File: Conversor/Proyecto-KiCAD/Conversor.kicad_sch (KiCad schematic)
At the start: 21 parts, among them J1 ConnPila, J2 ConnTrafoP, J3 ConnTrafoS, J4 ConnLf, J5 ConnCarga, Q1 IRFP150, Q2 IRFP150, Q3 IRFP150, Q4 IRFP150

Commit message: Comenzar a asignar footprints a todos los componentes
- Agregado un header para conectar el módulo de tarjeta SD de Arduino
por SPI
- Los GNDs conectados por resistencias nulas son para conectar los GNDs
en caso de que fuera necesario
- Agregar una nota de aplicaión de aislación para I2C (creo que como
estan conectados SDAO y SDAI está bien)
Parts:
- C1, C17, C2, C3, C4: footprint (none) -> Capacitor_SMD:C_1206_3216Metric_Pad1.33x1.80mm_HandSolder
- R7: footprint (none) -> Resistor_SMD:R_2512_6332Metric_Pad1.40x3.35mm_HandSolder
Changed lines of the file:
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@@
       (effects (font (size 1.27 1.27)) (justify left))
     )
-    (property "Footprint" "" (id 2) (at 105.41 113.03 0)
+    (property "Footprint" "Capacitor_SMD:C_1206_3216Metric_Pad1.33x1.80mm_HandSolder" (id 2) (at 105.41 113.03 0)
       (effects (font (size 1.27 1.27)) hide)
     )
@@
       (effects (font (size 1.27 1.27)) (justify left))
     )
-    (property "Footprint" "" (id 2) (at 154.94 113.03 0)
+    (property "Footprint" "Capacitor_SMD:C_1206_3216Metric_Pad1.33x1.80mm_HandSolder" (id 2) (at 154.94 113.03 0)
       (effects (font (size 1.27 1.27)) hide)
     )
@@
       (effects (font (size 1.27 1.27)) (justify left))
     )
-    (property "Footprint" "" (id 2) (at 154.94 87.63 0)
+    (property "Footprint" "Capacitor_SMD:C_1206_3216Metric_Pad1.33x1.80mm_HandSolder" (id 2) (at 154.94 87.63 0)
       (effects (font (size 1.27 1.27)) hide)
     )
@@
     (property "Reference" "C17" (id 0) (at 50.8063 76.2 90))
     (property "Value" "CS" (id 1) (at 50.8063 78.74 90))
-    (property "Footprint" "" (id 2) (at 50.8 82.55 0)
+    (property "Footprint" "Capacitor_SMD:C_1206_3216Metric_Pad1.33x1.80mm_HandSolder" (id 2) (at 50.8 82.55 0)
       (effects (font (size 1.27 1.27)) hide)
     )
@@
     (property "Reference" "R7" (id 0) (at 46.99 91.44 90))
     (property "Value" "RS" (id 1) (at 50.8 92.71 90))
-    (property "Footprint" "" (id 2) (at 50.8 91.948 90)
+    (property "Footprint" "Resistor_SMD:R_2512_6332Metric_Pad1.40x3.35mm_HandSolder" (id 2) (at 50.8 91.948 90)
       (effects (font (size 1.27 1.27)) hide)
     )
@@
       (effects (font (size 1.27 1.27)) (justify left))
     )
-    (property "Footprint" "" (id 2) (at 105.41 87.63 0)
-      (effects (font (size 1.27 1.27)) hide)
-    )
+    (property "Footprint" "Capacitor_SMD:C_1206_3216Metric_Pad1.33x1.80mm_HandSolder" (id 2) (at 105.41 87.63 0)
+      (effects (font (size 1.27 1.27)) hide)
+    )

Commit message: Comenzar el layout de componentes de la PCB
- Todos los componentes con footprints asignados (preliminar)
- Organizados los componentes de la placa adaptadora en el esquema del
PCB (usando como guia aproximada la placa adaptadora)
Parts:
- C5: footprint (none) -> Capacitor_THT:CP_Radial_D6.3mm_P2.50mm
- C6: footprint (none) -> Capacitor_THT:CP_Radial_D18.0mm_P7.50mm
- J1, J2, J3, J4, J5: footprint (none) -> TerminalBlock:TerminalBlock_bornier-2_P5.08mm
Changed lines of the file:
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@@
       (effects (font (size 1.27 1.27)) (justify right))
     )
-    (property "Footprint" "" (id 2) (at 67.31 99.06 0)
+    (property "Footprint" "Capacitor_THT:CP_Radial_D6.3mm_P2.50mm" (id 2) (at 67.31 99.06 0)
       (effects (font (size 1.27 1.27)) hide)
     )
@@
       (effects (font (size 1.27 1.27)) (justify left))
     )
-    (property "Footprint" "" (id 2) (at 29.21 97.79 0)
+    (property "Footprint" "TerminalBlock:TerminalBlock_bornier-2_P5.08mm" (id 2) (at 29.21 97.79 0)
       (effects (font (size 1.27 1.27)) hide)
     )
@@
       (effects (font (size 1.27 1.27)) (justify right))
     )
-    (property "Footprint" "" (id 2) (at 229.87 78.74 0)
+    (property "Footprint" "TerminalBlock:TerminalBlock_bornier-2_P5.08mm" (id 2) (at 229.87 78.74 0)
       (effects (font (size 1.27 1.27)) hide)
     )
@@
     (property "Reference" "J3" (id 0) (at 186.69 95.25 0))
     (property "Value" "ConnTrafoS" (id 1) (at 186.69 102.87 0))
-    (property "Footprint" "" (id 2) (at 186.69 97.79 0)
+    (property "Footprint" "TerminalBlock:TerminalBlock_bornier-2_P5.08mm" (id 2) (at 186.69 97.79 0)
       (effects (font (size 1.27 1.27)) hide)
     )
@@
       (effects (font (size 1.27 1.27)) (justify left))
     )
-    (property "Footprint" "" (id 2) (at 163.83 97.79 0)
+    (property "Footprint" "TerminalBlock:TerminalBlock_bornier-2_P5.08mm" (id 2) (at 163.83 97.79 0)
       (effects (font (size 1.27 1.27)) hide)
     )
@@
       (effects (font (size 1.27 1.27)) (justify left))
     )
-    (property "Footprint" "" (id 2) (at 270.51 99.06 0)
+    (property "Footprint" "TerminalBlock:TerminalBlock_bornier-2_P5.08mm" (id 2) (at 270.51 99.06 0)
       (effects (font (size 1.27 1.27)) hide)
     )
@@
       (effects (font (size 1.27 1.27)) (justify left))
     )
-    (property "Footprint" "" (id 2) (at 253.6952 104.14 0)
-      (effects (font (size 1.27 1.27)) hide)
-    )
+    (property "Footprint" "Capacitor_THT:CP_Radial_D18.0mm_P7.50mm" (id 2) (at 253.6952 104.14 0)
+      (effects (font (size 1.27 1.27)) hide)
+    )

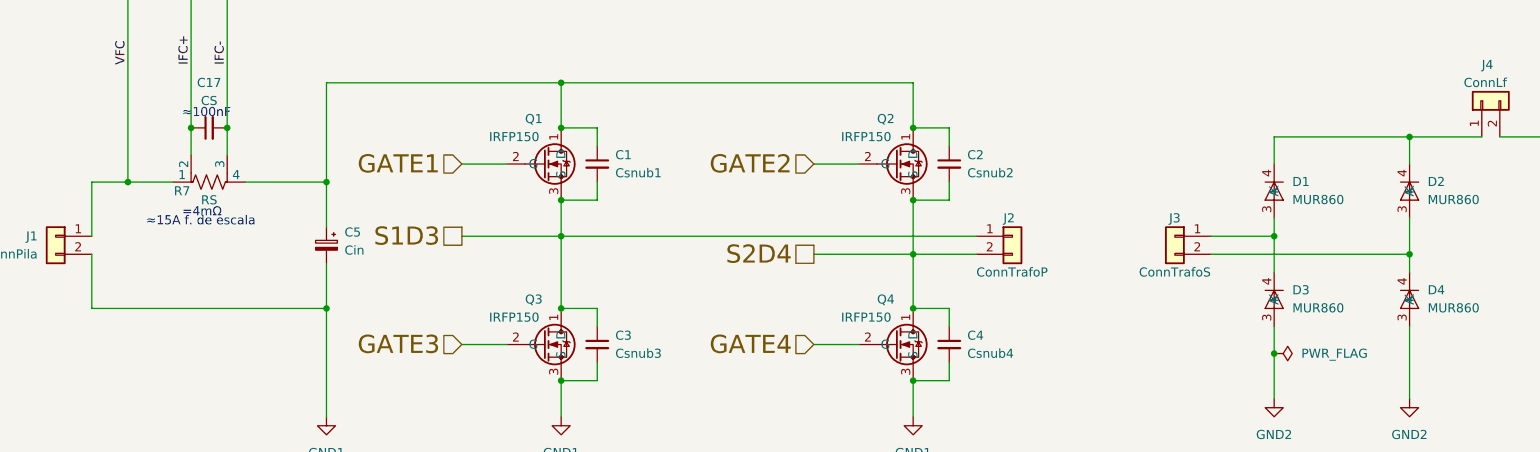
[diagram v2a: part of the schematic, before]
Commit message: Reempezar el ordenado de componentes del PCB
- Intentar copiar mas a la placa adaptadora en la parte del DSP (digital)
  - Algunas cosas (como los headers y la parte de USB) se movieron para hacer entrar mejor las cosas
- Layout bastante completo
- Agregados algunos modelos 3D faltantes
Por hacer:
  - Mover y reorganizar la parte del LM5056, porque tiene una pata que va al secundario, y ahora esta muy lejos del area de GND2
  - Ver como reorganizar un poco para que no queden esquinas vacias
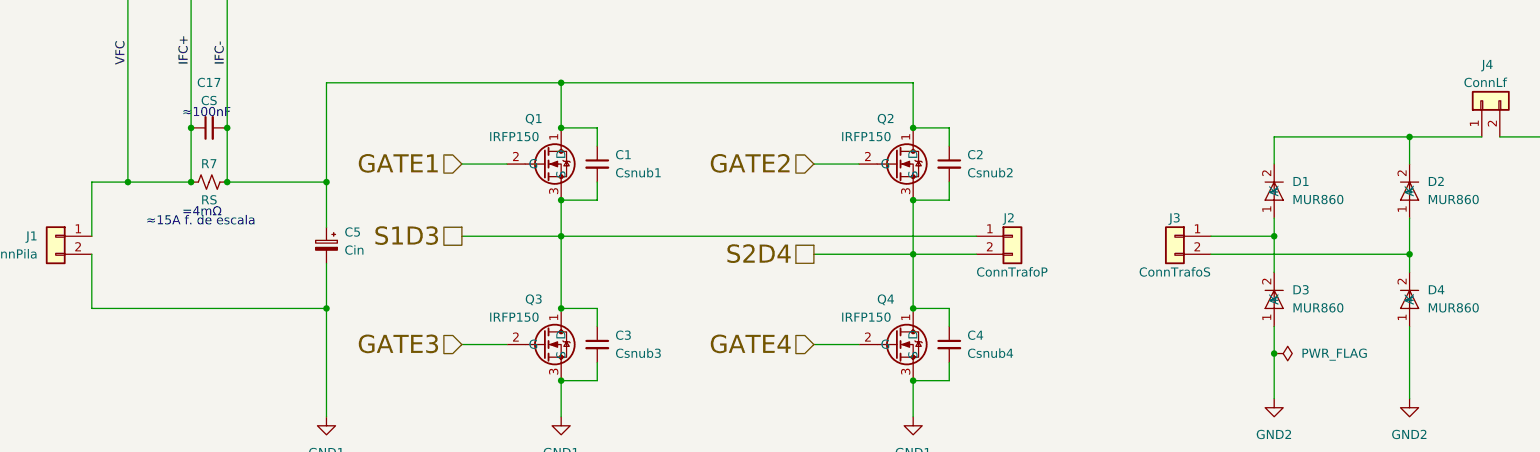
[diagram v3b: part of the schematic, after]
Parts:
- removed R7: RS, Resistor_SMD:R_2512_6332Metric_Pad1.40x3.35mm_HandSolder, symbol Device:R_Shunt_US
- added R7: RS, Resistor_SMD:R_2512_6332Metric_Pad1.40x3.35mm_HandSolder, symbol Device:R_Small_US
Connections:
- net VFC is gone; now on net IFC+: J1.1 (Pin_1)
- net GND2: now also D3.1 (A), D4.1 (A); no longer D3.3 (A), D4.3 (A)
- net IFC+: now also R7.1
- net IFC-: now also C1.1, C2.1, C5.1, Q1.1 (D), Q2.1 (D), R7.2
- new net: D1.1 (A), D3.2 (K), J3.1 (Pin_1)
- new net: D1.2 (K), D2.2 (K), J4.1 (Pin_1)
- new net: D2.1 (A), D4.2 (K), J3.2 (Pin_2)
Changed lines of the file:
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@@
 (kicad_sch (version 20211123) (generator eeschema)
   (paper "A4")
+  (junction (at 53.34 90.17) (diameter 0) (color 0 0 0 0)
+  )
+  (junction (at 48.26 90.17) (diameter 0) (color 0 0 0 0)
+  )
   (junction (at 67.31 90.17) (diameter 0) (color 0 0 0 0)
   )
@@
     (stroke (width 0) (type default) (color 0 0 0 0))
   )
-  (wire (pts (xy 39.37 90.17) (xy 45.72 90.17))
+  (wire (pts (xy 39.37 90.17) (xy 48.26 90.17))
     (stroke (width 0) (type default) (color 0 0 0 0))
   )
@@
     (stroke (width 0) (type default) (color 0 0 0 0))
   )
-  (wire (pts (xy 55.88 90.17) (xy 67.31 90.17))
+  (wire (pts (xy 53.34 90.17) (xy 67.31 90.17))
     (stroke (width 0) (type default) (color 0 0 0 0))
   )
@@
     (stroke (width 0) (type default) (color 0 0 0 0))
   )
-  (wire (pts (xy 48.26 82.55) (xy 48.26 86.36))
+  (wire (pts (xy 48.26 82.55) (xy 48.26 90.17))
     (stroke (width 0) (type default) (color 0 0 0 0))
   )
@@
     (stroke (width 0) (type default) (color 0 0 0 0))
   )
-  (wire (pts (xy 53.34 82.55) (xy 53.34 86.36))
+  (wire (pts (xy 53.34 82.55) (xy 53.34 90.17))
     (stroke (width 0) (type default) (color 0 0 0 0))
   )
@@
     (pin "2")
   )
+  (symbol (lib_id "Device:R_Small_US") (at 50.8 90.17 90) (unit 1)
+    (in_bom yes) (on_board yes)
+    (property "Reference" "R7" (id 0) (at 50.8 87.63 90))
+    (property "Value" "RS" (id 1) (at 50.8 92.71 90))
+    (property "Footprint" "Resistor_SMD:R_2512_6332Metric_Pad1.40x3.35mm_HandSolder" (id 2) (at 50.8 90.17 0)
+      (effects (font (size 1.27 1.27)) hide)
+    )
+    (property "Datasheet" "~" (id 3) (at 50.8 90.17 0)
+      (effects (font (size 1.27 1.27)) hide)
+    )
+    (pin "1")
+    (pin "2")
+  )
   (symbol (lib_id "power:GND2") (at 252.73 120.65 0) (unit 1)
     (in_bom yes) (on_board yes) (fields_autoplaced)
@@
       (effects (font (size 1.27 1.27)) hide)
     )
-    (pin "3")
-    (pin "4")
-  )
-  (symbol (lib_id "Componentes proyecto:MUR860") (at 200.66 91.44 0) (unit 1)
+    (pin "1")
+    (pin "2")
+  )
+  (symbol (lib_name "MUR860_1") (lib_id "Componentes proyecto:MUR860") (at 200.66 91.44 0) (unit 1)
     (in_bom yes) (on_board yes) (fields_autoplaced)
     (property "Reference" "D1" (id 0) (at 203.2 90.1318 0)
@@
       (effects (font (size 1.27 1.27)) hide)
     )
-    (pin "3")
-    (pin "4")
+    (pin "1")
+    (pin "2")
   )
   (symbol (lib_id "power:GND2") (at 265.43 120.65 0) (unit 1)
@@
     (pin "2")
   )
-  (symbol (lib_id "Componentes proyecto:MUR860") (at 219.71 91.44 0) (unit 1)
+  (symbol (lib_name "MUR860_2") (lib_id "Componentes proyecto:MUR860") (at 219.71 91.44 0) (unit 1)
     (in_bom yes) (on_board yes) (fields_autoplaced)
     (property "Reference" "D2" (id 0) (at 222.25 90.1318 0)
@@
       (effects (font (size 1.27 1.27)) hide)
     )
-    (pin "3")
-    (pin "4")
-  )
-  (symbol (lib_id "Device:R_Shunt_US") (at 50.8 90.17 90) (unit 1)
-    (in_bom yes) (on_board yes)
-    (property "Reference" "R7" (id 0) (at 46.99 91.44 90))
-    (property "Value" "RS" (id 1) (at 50.8 92.71 90))
-    (property "Footprint" "Resistor_SMD:R_2512_6332Metric_Pad1.40x3.35mm_HandSolder" (id 2) (at 50.8 91.948 90)
-      (effects (font (size 1.27 1.27)) hide)
-    )
-    (property "Datasheet" "~" (id 3) (at 50.8 90.17 0)
-      (effects (font (size 1.27 1.27)) hide)
-    )
-    (pin "1")
-    (pin "2")
-    (pin "3")
-    (pin "4")
+    (pin "1")
+    (pin "2")
   )
   (symbol (lib_id "power:GND1") (at 149.86 123.19 0) (unit 1)
@@
     (pin "2")
   )
-  (symbol (lib_id "Componentes proyecto:MUR860") (at 219.71 106.68 0) (unit 1)
+  (symbol (lib_name "MUR860_3") (lib_id "Componentes proyecto:MUR860") (at 219.71 106.68 0) (unit 1)
     (in_bom yes) (on_board yes) (fields_autoplaced)
     (property "Reference" "D4" (id 0) (at 222.25 105.3718 0)
@@
       (effects (font (size 1.27 1.27)) hide)
     )
-    (pin "3")
-    (pin "4")
+    (pin "1")
+    (pin "2")
   )
   (symbol (lib_id "Device:C_Small") (at 105.41 87.63 0) (unit 1)

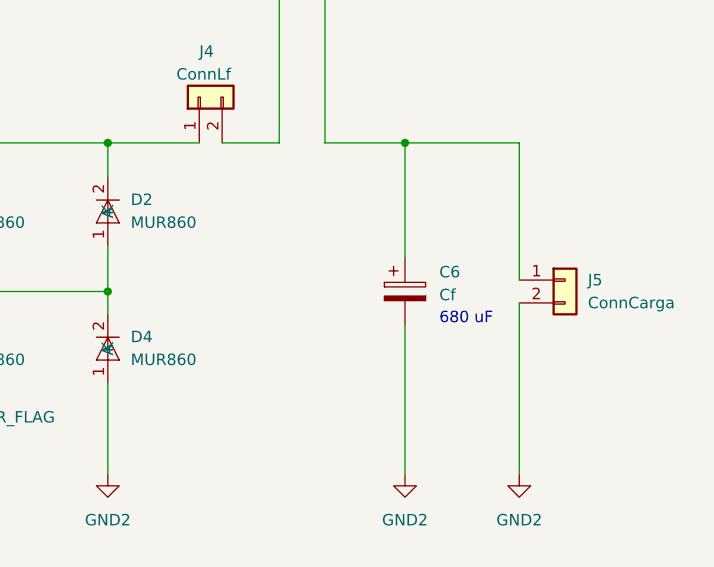
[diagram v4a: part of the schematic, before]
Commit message: Continuar con el diseño de la PCB
- Agregar los agujeros de tornillos
- Terminar la parte del secundario
- Agregar el borde en Egde.cuts que causaba problema
- Corregir las pista que no entran derechas a los pads
- Cambiar las footprints de los conectores
Por hacer:
  - Consultar de componentes como headers a Claus
  - Una vez terminada pedir cotización en las paginas que me pasó Jorge (Bookmarks de Firefox)
  - Ver de agrear un selector para la alimentación externa por header en la entrada de 12-18V (preguntar a Claus)
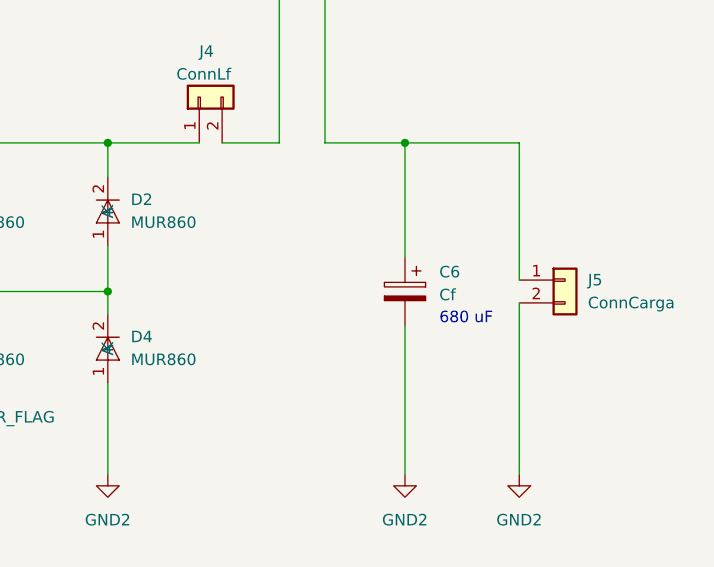
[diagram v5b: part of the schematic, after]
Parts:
- C5: footprint Capacitor_THT:CP_Radial_D6.3mm_P2.50mm -> Capacitor_THT:CP_Radial_D12.5mm_P5.00mm
- J1, J2, J3, J4, J5: footprint TerminalBlock:TerminalBlock_bornier-2_P5.08mm -> TerminalBlock:TerminalBlock_Wuerth_691311400102_P7.62mm
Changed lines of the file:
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@@
       (effects (font (size 1.27 1.27)) (justify right))
     )
-    (property "Footprint" "Capacitor_THT:CP_Radial_D6.3mm_P2.50mm" (id 2) (at 67.31 99.06 0)
+    (property "Footprint" "Capacitor_THT:CP_Radial_D12.5mm_P5.00mm" (id 2) (at 67.31 99.06 0)
       (effects (font (size 1.27 1.27)) hide)
     )
@@
       (effects (font (size 1.27 1.27)) (justify left))
     )
-    (property "Footprint" "TerminalBlock:TerminalBlock_bornier-2_P5.08mm" (id 2) (at 29.21 97.79 0)
+    (property "Footprint" "TerminalBlock:TerminalBlock_Wuerth_691311400102_P7.62mm" (id 2) (at 29.21 97.79 0)
       (effects (font (size 1.27 1.27)) hide)
     )
@@
       (effects (font (size 1.27 1.27)) (justify right))
     )
-    (property "Footprint" "TerminalBlock:TerminalBlock_bornier-2_P5.08mm" (id 2) (at 229.87 78.74 0)
+    (property "Footprint" "TerminalBlock:TerminalBlock_Wuerth_691311400102_P7.62mm" (id 2) (at 229.87 78.74 0)
       (effects (font (size 1.27 1.27)) hide)
     )
@@
     (property "Reference" "J3" (id 0) (at 186.69 95.25 0))
     (property "Value" "ConnTrafoS" (id 1) (at 186.69 102.87 0))
-    (property "Footprint" "TerminalBlock:TerminalBlock_bornier-2_P5.08mm" (id 2) (at 186.69 97.79 0)
+    (property "Footprint" "TerminalBlock:TerminalBlock_Wuerth_691311400102_P7.62mm" (id 2) (at 186.69 97.79 0)
       (effects (font (size 1.27 1.27)) hide)
     )
@@
       (effects (font (size 1.27 1.27)) (justify left))
     )
-    (property "Footprint" "TerminalBlock:TerminalBlock_bornier-2_P5.08mm" (id 2) (at 163.83 97.79 0)
+    (property "Footprint" "TerminalBlock:TerminalBlock_Wuerth_691311400102_P7.62mm" (id 2) (at 163.83 97.79 0)
       (effects (font (size 1.27 1.27)) hide)
     )
@@
       (effects (font (size 1.27 1.27)) (justify left))
     )
-    (property "Footprint" "TerminalBlock:TerminalBlock_bornier-2_P5.08mm" (id 2) (at 270.51 99.06 0)
+    (property "Footprint" "TerminalBlock:TerminalBlock_Wuerth_691311400102_P7.62mm" (id 2) (at 270.51 99.06 0)
       (effects (font (size 1.27 1.27)) hide)
     )
@@
     (pin "3")
   )
-  (symbol (lib_id "Device:C_Polarized") (at 252.73 100.33 0) (unit 1)
+  (symbol (lib_id "Device:C_Polarized") (at 252.73 100.33 0) (mirror y) (unit 1)
     (in_bom yes) (on_board yes) (fields_autoplaced)
     (property "Reference" "C6" (id 0) (at 256.54 98.1709 0)
-      (effects (font (size 1.27 1.27)) (justify left))
+      (effects (font (size 1.27 1.27)) (justify right))
     )
     (property "Value" "Cf" (id 1) (at 256.54 100.7109 0)
-      (effects (font (size 1.27 1.27)) (justify left))
-    )
-    (property "Footprint" "Capacitor_THT:CP_Radial_D18.0mm_P7.50mm" (id 2) (at 253.6952 104.14 0)
-      (effects (font (size 1.27 1.27)) hide)
-    )
+      (effects (font (size 1.27 1.27)) (justify right))
+    )
+    (property "Footprint" "Capacitor_THT:CP_Radial_D18.0mm_P7.50mm" (id 2) (at 251.7648 104.14 0)
+      (effects (font (size 1.27 1.27)) hide)
+    )

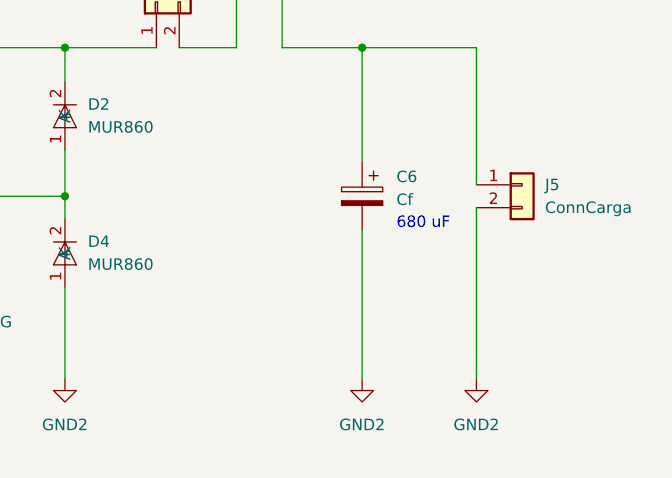
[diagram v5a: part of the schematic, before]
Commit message: Terminar de rutear todas las pistas de cobre de la placa
- Pistas de 4.5mm para las partes de 9A (primario) y 2mm para las de 4A (secundario)
- Agregar doble capacitor en serie a la salida, para disminuir los requerimientos de tensión de cada capacitor
  - Falta ver si es necesario a la entrada
- Agregar el circuito de medición de corriente a la entrada como recomienda la hoja de datos del LM5056
- Agregar modelos 3D de los conectores (sacados de Irusta-Caravelli)
Por hacer:
  - Preguntar por los componentes disponibles a Claus
  - Ver como entran los disipadores para MOSFETs y diodos
  - Asegurarse de la conexión de las dos líneas de datos de I2C despues del aislador
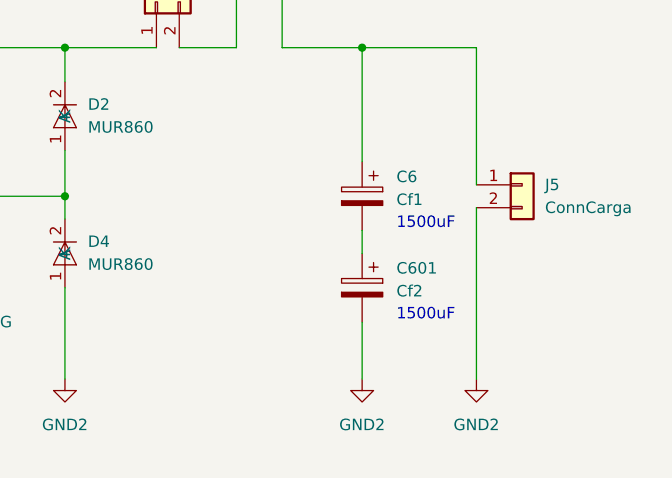
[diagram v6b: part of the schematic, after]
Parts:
- added C601: Cf2, Capacitor_THT:CP_Radial_D18.0mm_P7.50mm, symbol Device:C_Polarized
- C6: value Cf -> Cf1
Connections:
- net GND2: now also C601.2; no longer C6.2
- new net: C6.2, C601.1
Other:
- note added: "1500uF"
- note removed: "680 uF"
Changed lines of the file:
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@@
+    (stroke (width 0) (type default) (color 0 0 0 0))
+  )
+  (wire (pts (xy 252.73 114.3) (xy 252.73 120.65))
     (stroke (width 0) (type default) (color 0 0 0 0))
   )
@@
     (stroke (width 0) (type default) (color 0 0 0 0))
   )
-  (wire (pts (xy 252.73 104.14) (xy 252.73 120.65))
+  (wire (pts (xy 252.73 104.14) (xy 252.73 106.68))
     (stroke (width 0) (type default) (color 0 0 0 0))
   )
@@
     (effects (font (size 1.27 1.27)) (justify left bottom))
   )
-  (text "680 uF" (at 256.54 104.14 0)
+  (text "1500uF" (at 256.54 104.14 0)
     (effects (font (size 1.27 1.27)) (justify left bottom))
   )
   (text "≈15A f. de escala" (at 41.91 96.52 0)
+    (effects (font (size 1.27 1.27)) (justify left bottom))
+  )
+  (text "1500uF" (at 256.54 114.3 0)
     (effects (font (size 1.27 1.27)) (justify left bottom))
   )
@@
     (pin "3")
   )
+  (symbol (lib_id "Device:C_Polarized") (at 252.73 110.49 0) (mirror y) (unit 1)
+    (in_bom yes) (on_board yes) (fields_autoplaced)
+    (property "Reference" "C601" (id 0) (at 256.54 108.3309 0)
+      (effects (font (size 1.27 1.27)) (justify right))
+    )
+    (property "Value" "Cf2" (id 1) (at 256.54 110.8709 0)
+      (effects (font (size 1.27 1.27)) (justify right))
+    )
+    (property "Footprint" "Capacitor_THT:CP_Radial_D18.0mm_P7.50mm" (id 2) (at 251.7648 114.3 0)
+      (effects (font (size 1.27 1.27)) hide)
+    )
+    (property "Datasheet" "~" (id 3) (at 252.73 110.49 0)
+      (effects (font (size 1.27 1.27)) hide)
+    )
+    (pin "1")
+    (pin "2")
+  )
   (symbol (lib_id "Device:C_Polarized") (at 252.73 100.33 0) (mirror y) (unit 1)
     (in_bom yes) (on_board yes) (fields_autoplaced)
@@
       (effects (font (size 1.27 1.27)) (justify right))
     )
-    (property "Value" "Cf" (id 1) (at 256.54 100.7109 0)
-      (effects (font (size 1.27 1.27)) (justify right))
-    )
+    (property "Value" "Cf1" (id 1) (at 256.54 100.7109 0)
+      (effects (font (size 1.27 1.27)) (justify right))
+    )
